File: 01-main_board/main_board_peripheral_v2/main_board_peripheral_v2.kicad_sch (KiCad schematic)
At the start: 20 parts, among them J2 T4040014041000, J3 T4041017041-000, J4 FH41-15S-0.5SH_05_, Q1 SSF2302, U1 LM74610QDGKRQ1

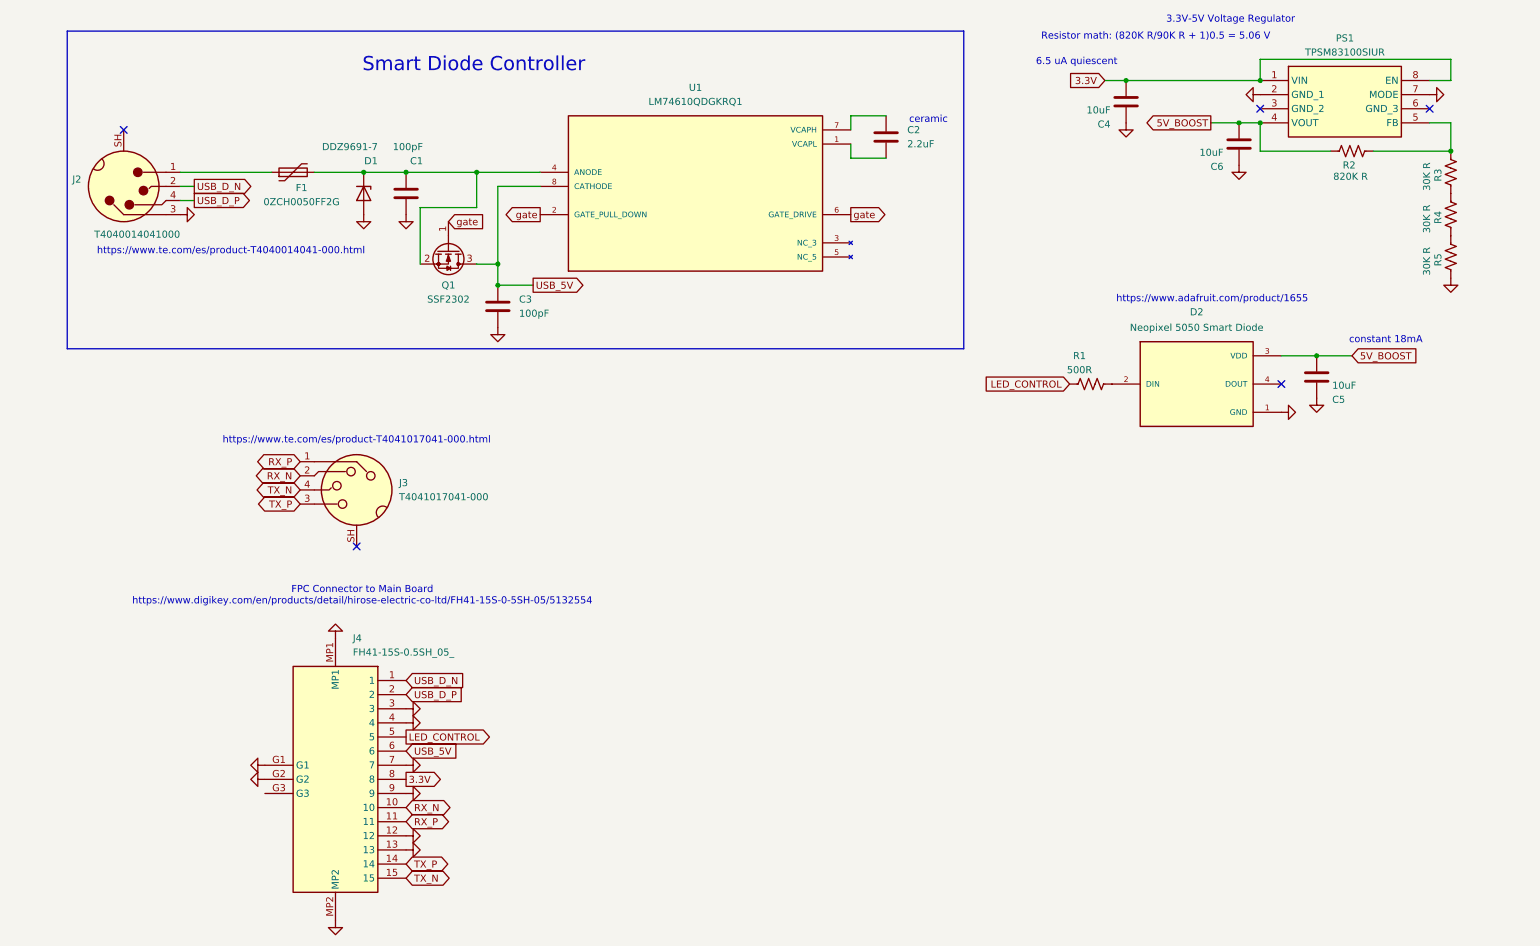
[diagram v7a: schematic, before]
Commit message: Started new layout on version 3
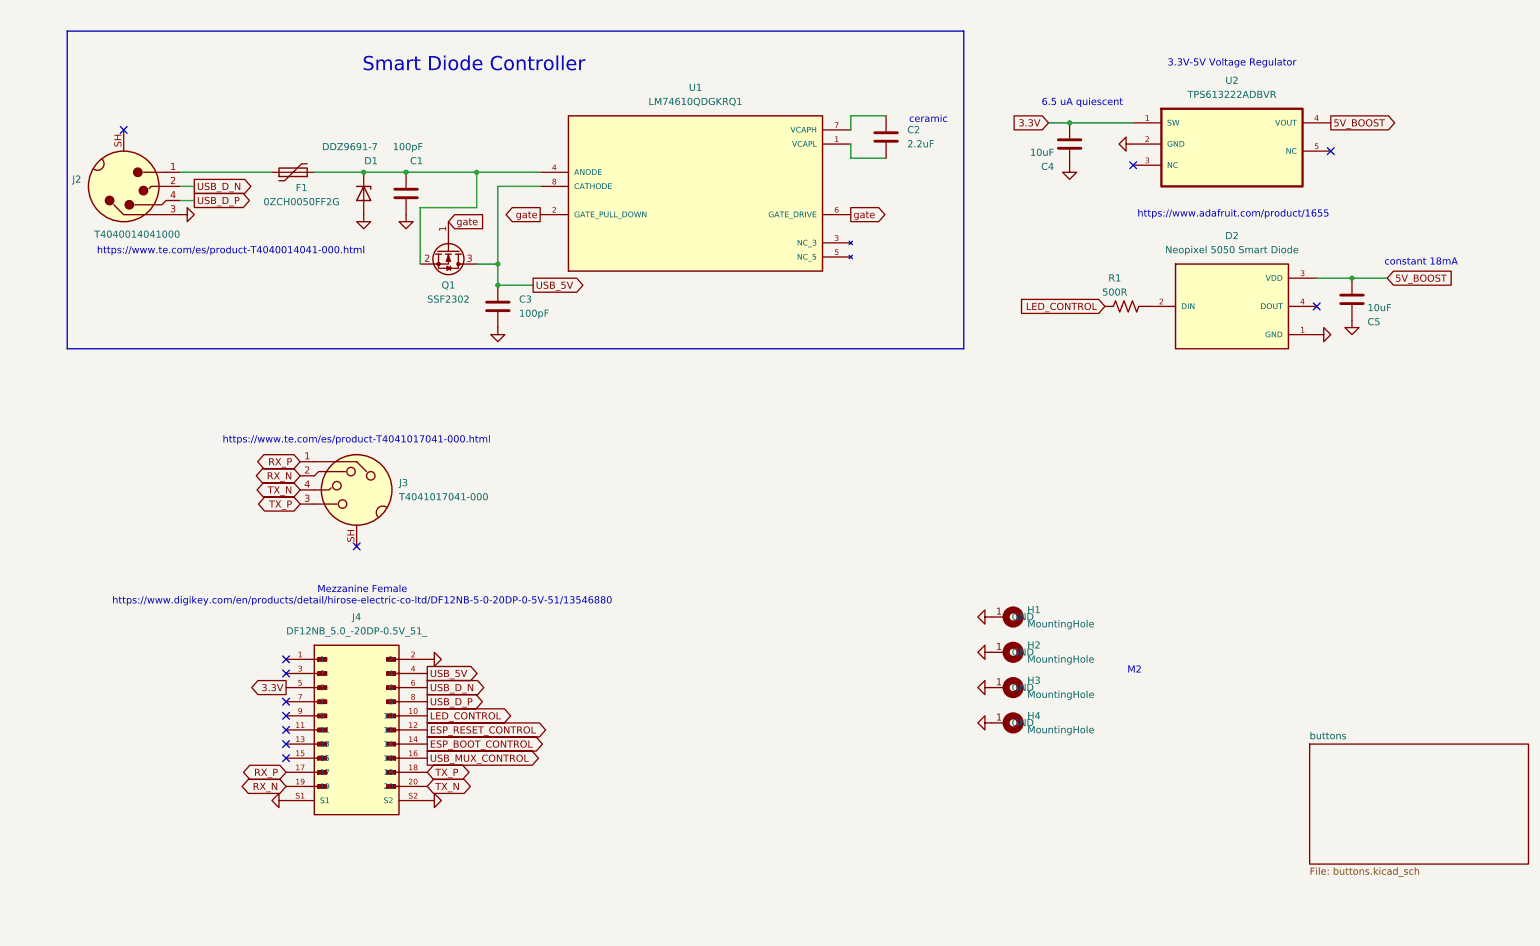
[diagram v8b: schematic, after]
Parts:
- removed C6: 10uF, Capacitor_SMD:C_0603_1608Metric, symbol Device:C
- removed J4: FH41-15S-0.5SH_05_, 22XT_Main_Peripheral:FH4115S05SH05, symbol FH41-15S-0_5SH_05_:FH41-15S-0.5SH_05_
- removed PS1: TPSM83100SIUR, 22XT_Main_Peripheral:TPSM83100SIUR, symbol 2026-02-06_01-22-38:TPSM83100SIUR
- removed R2: 820K R, 22XT_Main_Peripheral:RESC3116X65N (820K), symbol Device:R_US
- removed R3, R4, R5: 30K R, 22XT_Main_Peripheral:RESC3116X65N (30K), symbol Device:R_US
- added H1, H2, H3, H4: MountingHole, MountingHole:MountingHole_2.2mm_M2_Pad, symbol Mechanical:MountingHole
- added J4: DF12NB_5.0_-20DP-0.5V_51_, 22XT_Main_Peripheral:DF12NB_5.0_-20DP-0.5V_51_, symbol DF12NB_5.0_-20DP-0.5V_51_:DF12NB_5.0_-20DP-0.5V_51_
- added U2: TPS613222ADBVR, 22XT_Main_Peripheral:TPS613222ADBVR, symbol TPS613222ADBVR:TPS613222ADBVR
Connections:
- net 3.3V: now also J4.5, U2.1 (SW)
- net 5V_BOOST: now also U2.4 (VOUT)
- net GND: now also H1.1 (GND), H2.1 (GND), H3.1 (GND), H4.1 (GND), J4.2, J4.S1, J4.S2, U2.2 (GND)
- net LED_CONTROL: now also J4.10
- net RX_N: now also J4.19
- net RX_P: now also J4.17
- net TX_N: now also J4.20
- net TX_P: now also J4.18
- net USB_5V: now also J4.4
- net USB_D_N: now also J4.6
- net USB_D_P: now also J4.8
- new net ESP_BOOT_CONTROL: J4.14
- new net ESP_RESET_CONTROL: J4.12
- new net USB_MUX_CONTROL: J4.16
- no-connect marks 5 -> 12
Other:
- added sheet buttons (buttons.kicad_sch)
- note added: "M2"
- note added: "Mezzanine Female https://www.digikey.com/en/products/detail/hirose-electric-co-ltd/DF12NB-5-0-20DP-0-5V-51/13546880"
- note removed: "FPC Connector to Main Board https://www.digikey.com/en/products/detail/hirose-electric-co-ltd/FH41-15S-0-5SH-05/5132554"
- note removed: "Resistor math: (820K R/90K R + 1)0.5 = 5.06 V"
- moved on the sheet: C4, C5, D2, R1
